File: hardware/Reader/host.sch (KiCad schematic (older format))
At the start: 7 parts

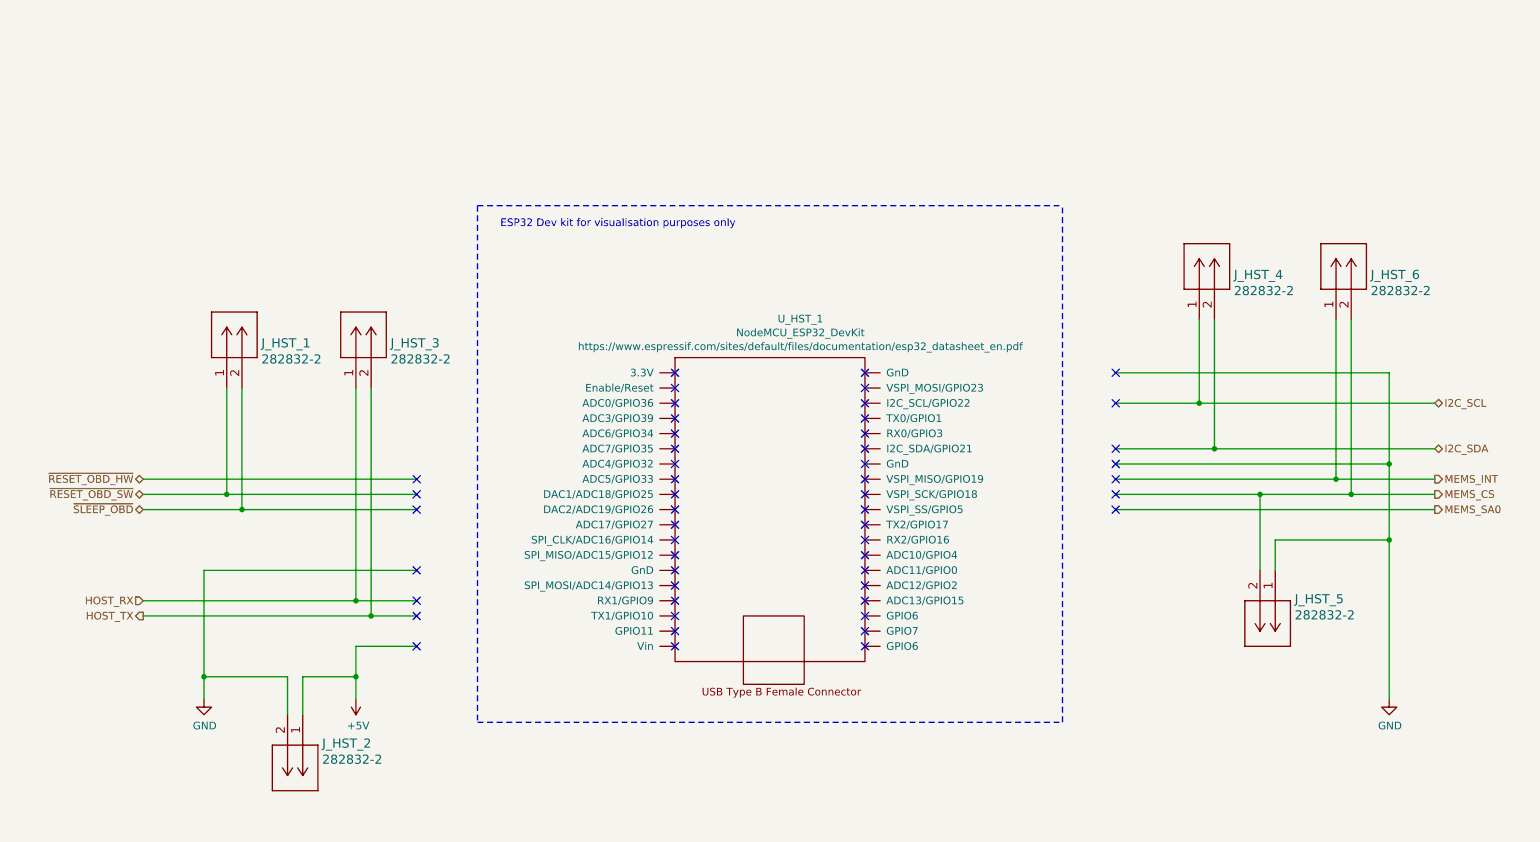
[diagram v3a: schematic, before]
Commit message: Fixed minor bugs in schematic. Completed PCB layout v0.0.1 and exported Gerber files
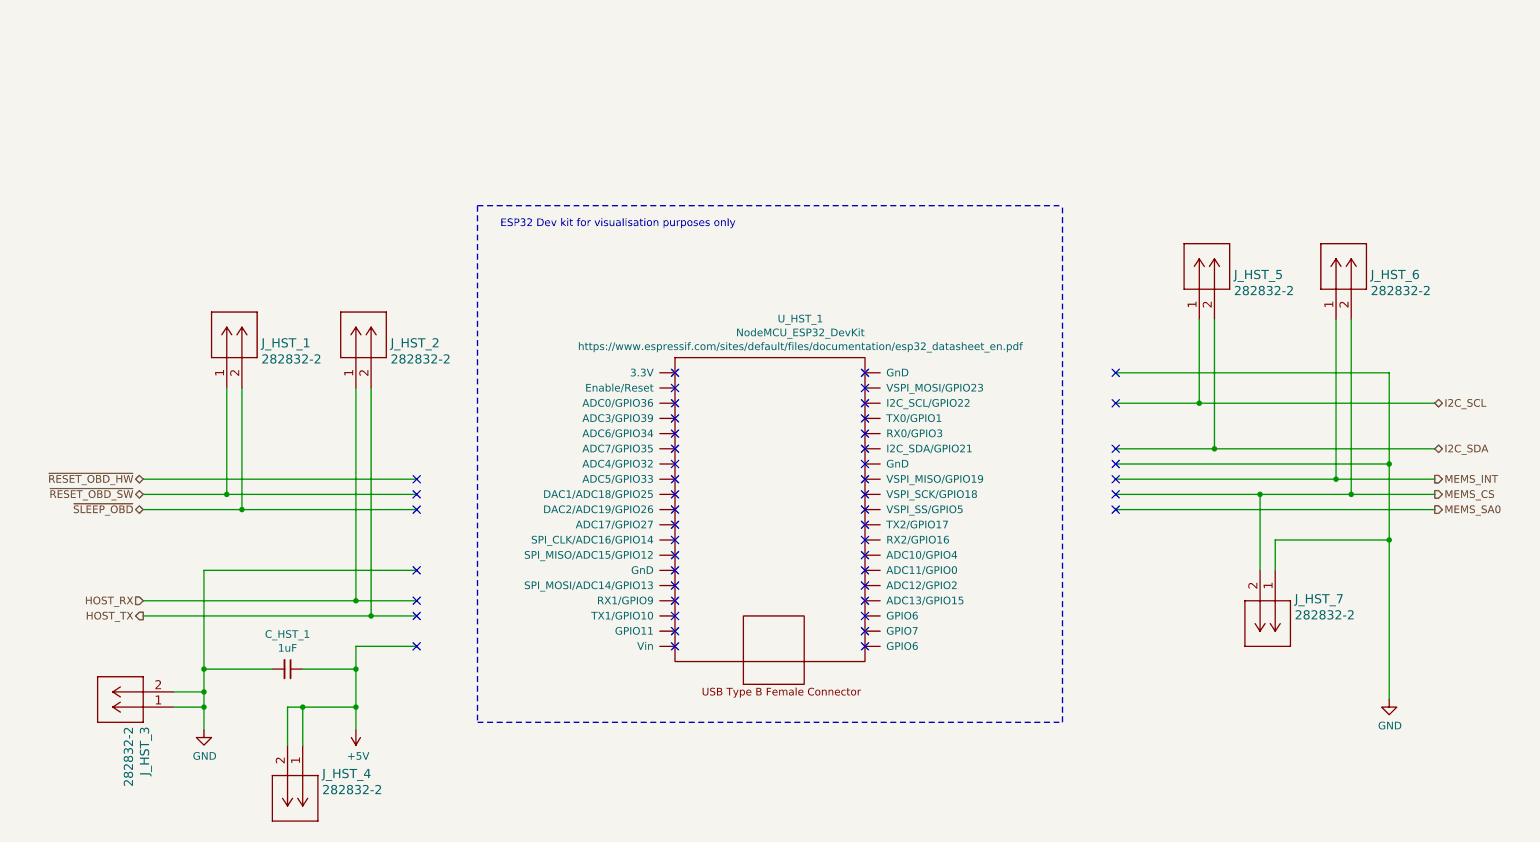
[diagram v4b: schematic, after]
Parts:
- added C_HST_1: 1uF, footprints:0603, symbol Device:C_Small
- added J_HST_3: 282832-2, footprints:282832-2, symbol 2828322:282832-2
- renumbered J_HST_3 to J_HST_2, J_HST_2 to J_HST_4, J_HST_4 to J_HST_5, J_HST_5 to J_HST_7
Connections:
- net +5V: now also J_HST_4.2, C_HST_1.1
- net GND: now also C_HST_1.2, J_HST_3.1, J_HST_3.2; no longer J_HST_4.2
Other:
- moved on the sheet: J_HST_4
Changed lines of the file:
@@
 Sheet 13 19
 Title "CANnect Reader | Host"
-Date "2020-10-25"
+Date "2020-10-27"
 Rev "0.0.03"
 Comp "CANtech"
@@
 L power:GND #PWR084
 U 1 1 5F91E8F3
-P 1800 5400
-F 0 "#PWR084" H 1800 5150 50  0001 C CNN
-F 1 "GND" H 1805 5227 50  0000 C CNN
-F 2 "" H 1800 5400 50  0001 C CNN
-F 3 "" H 1800 5400 50  0001 C CNN
-	1    1800 5400
+P 1800 5600
+F 0 "#PWR084" H 1800 5350 50  0001 C CNN
+F 1 "GND" H 1805 5427 50  0000 C CNN
+F 2 "" H 1800 5600 50  0001 C CNN
+F 3 "" H 1800 5600 50  0001 C CNN
+	1    1800 5600
 	1    0    0    -1
 $EndComp
-Wire Wire Line
-	1800 5400 1800 5250
 $Comp
 L power:+5V #PWR085
 U 1 1 5F91DA5E
-P 2800 5400
-F 0 "#PWR085" H 2800 5250 50  0001 C CNN
-F 1 "+5V" H 2815 5573 50  0000 C CNN
-F 2 "" H 2800 5400 50  0001 C CNN
-F 3 "" H 2800 5400 50  0001 C CNN
-	1    2800 5400
+P 2800 5600
+F 0 "#PWR085" H 2800 5450 50  0001 C CNN
+F 1 "+5V" H 2815 5773 50  0000 C CNN
+F 2 "" H 2800 5600 50  0001 C CNN
+F 3 "" H 2800 5600 50  0001 C CNN
+	1    2800 5600
 	1    0    0    1
 $EndComp
 Wire Wire Line
-	2800 5400 2800 5250
+	2800 5600 2800 5450
 $Comp
 L CANtech:NodeMCU_ESP32_DevKit U_HST_?
@@
 $EndComp
 Wire Wire Line
-	2800 5050 3200 5050
-Wire Wire Line
 	1800 4550 3200 4550
 NoConn ~ 3200 3950
@@
 $EndComp
 $Comp
-L 2828322:282832-2 J_HST_3
+L 2828322:282832-2 J_HST_2
 U 1 1 5F9D9258
 P 2800 3350
-F 0 "J_HST_3" V 3095 3122 60  0000 R CNN
+F 0 "J_HST_2" V 3095 3122 60  0000 R CNN
 F 1 "282832-2" V 2989 3122 60  0000 R CNN
 F 2 "footprints:282832-2" H 3200 3290 60  0001 C CNN
@@
 $EndComp
 $Comp
-L 2828322:282832-2 J_HST_2
+L 2828322:282832-2 J_HST_4
 U 1 1 5F9D9519
-P 2450 5500
-F 0 "J_HST_2" V 2639 5628 60  0000 L CNN
-F 1 "282832-2" V 2745 5628 60  0000 L CNN
-F 2 "footprints:282832-2" H 2850 5440 60  0001 C CNN
-F 3 "https://www.te.com/commerce/DocumentDelivery/DDEController?Action=srchrtrv&DocNm=282832&DocType=Customer+Drawing&DocLang=English" H 2450 5500 60  0001 C CNN
-F 4 "282832-2" H 2450 5500 50  0001 C CNN "Part Name"
-F 5 "DigiKey Canada" H 2450 5500 50  0001 C CNN "Vendor"
-F 6 "TE Connectivity AMP Connectors" H 2450 5500 50  0001 C CNN "Manufacturer"
-F 7 "A113314-ND" H 2450 5500 50  0001 C CNN "digikeypn"
-	1    2450 5500
+P 2450 5700
+F 0 "J_HST_4" V 2639 5828 60  0000 L CNN
+F 1 "282832-2" V 2745 5828 60  0000 L CNN
+F 2 "footprints:282832-2" H 2850 5640 60  0001 C CNN
+F 3 "https://www.te.com/commerce/DocumentDelivery/DDEController?Action=srchrtrv&DocNm=282832&DocType=Customer+Drawing&DocLang=English" H 2450 5700 60  0001 C CNN
+F 4 "282832-2" H 2450 5700 50  0001 C CNN "Part Name"
+F 5 "DigiKey Canada" H 2450 5700 50  0001 C CNN "Vendor"
+F 6 "TE Connectivity AMP Connectors" H 2450 5700 50  0001 C CNN "Manufacturer"
+F 7 "A113314-ND" H 2450 5700 50  0001 C CNN "digikeypn"
+	1    2450 5700
 	0    1    1    0
 $EndComp
 $Comp
-L 2828322:282832-2 J_HST_4
+L 2828322:282832-2 J_HST_5
 U 1 1 5F9DA91B
 P 8350 2900
-F 0 "J_HST_4" V 8645 2672 60  0000 R CNN
+F 0 "J_HST_5" V 8645 2672 60  0000 R CNN
 F 1 "282832-2" V 8539 2672 60  0000 R CNN
 F 2 "footprints:282832-2" H 8750 2840 60  0001 C CNN
@@
 NoConn ~ 7800 3950
 Wire Wire Line
-	2450 5500 2450 5250
-Wire Wire Line
-	2450 5250 2800 5250
-Connection ~ 2800 5250
-Wire Wire Line
-	2800 5250 2800 5050
-Wire Wire Line
-	2350 5500 2350 5250
-Wire Wire Line
-	2350 5250 1800 5250
-Connection ~ 1800 5250
-Wire Wire Line
-	1800 5250 1800 4550
+	2450 5700 2450 5450
 Wire Notes Line
 	3600 2150 3600 5550
@@
 	7800 4150 9900 4150
 $Comp
-L 2828322:282832-2 J_HST_5
+L 2828322:282832-2 J_HST_7
 U 1 1 5F9F4BEC
 P 8850 4550
-F 0 "J_HST_5" V 9039 4678 60  0000 L CNN
+F 0 "J_HST_7" V 9039 4678 60  0000 L CNN
 F 1 "282832-2" V 9145 4678 60  0000 L CNN
 F 2 "footprints:282832-2" H 9250 4490 60  0001 C CNN
@@
 NoConn ~ 6150 3350
 NoConn ~ 6150 3250
+$Comp
+L Device:C_Small C_HST_1
+U 1 1 5FB5FEEA
+P 2350 5200
+F 0 "C_HST_1" V 2121 5200 50  0000 C CNN
+F 1 "1uF" V 2212 5200 50  0000 C CNN
+F 2 "footprints:0603" H 2350 5200 50  0001 C CNN
+F 3 "https://content.kemet.com/datasheets/KEM_C1002_X7R_SMD.pdf" H 2350 5200 50  0001 C CNN
+F 4 "Kermet" H 2350 5200 50  0001 C CNN "Manufacturer"
+F 5 "C0603C105K4RACTU" H 2350 5200 50  0001 C CNN "Part Name"
+F 6 "DigiKey Canada" H 2350 5200 50  0001 C CNN "Vendor"
+F 7 "399-7847-1-ND" H 2350 5200 50  0001 C CNN "digikeypn"
+	1    2350 5200
+	0    1    1    0
+$EndComp
+Wire Wire Line
+	2800 5050 3200 5050
+Wire Wire Line
+	2450 5450 2800 5450
+Wire Wire Line
+	1800 4550 1800 5200
+Wire Wire Line
+	2800 5050 2800 5200
+Connection ~ 2800 5450
+$Comp
+L 2828322:282832-2 J_HST_3
+U 1 1 5FB693E7
+P 1600 5450
+F 0 "J_HST_3" V 1789 5578 60  0000 L CNN
+F 1 "282832-2" V 1895 5578 60  0000 L CNN
+F 2 "footprints:282832-2" H 2000 5390 60  0001 C CNN
+F 3 "https://www.te.com/commerce/DocumentDelivery/DDEController?Action=srchrtrv&DocNm=282832&DocType=Customer+Drawing&DocLang=English" H 1600 5450 60  0001 C CNN
+F 4 "282832-2" H 1600 5450 50  0001 C CNN "Part Name"
+F 5 "DigiKey Canada" H 1600 5450 50  0001 C CNN "Vendor"
+F 6 "TE Connectivity AMP Connectors" H 1600 5450 50  0001 C CNN "Manufacturer"
+F 7 "A113314-ND" H 1600 5450 50  0001 C CNN "digikeypn"
+	1    1600 5450
+	-1   0    0    1
+$EndComp
+Wire Wire Line
+	1600 5450 1800 5450
+Connection ~ 1800 5450
+Wire Wire Line
+	1800 5450 1800 5600
+Wire Wire Line
+	2450 5200 2800 5200
+Connection ~ 2800 5200
+Wire Wire Line
+	2800 5200 2800 5450
+Wire Wire Line
+	2250 5200 1800 5200
+Connection ~ 1800 5200
+Wire Wire Line
+	1800 5200 1800 5350
+Wire Wire Line
+	1600 5350 1800 5350
+Connection ~ 1800 5350
+Wire Wire Line
+	1800 5350 1800 5450
+Wire Wire Line
+	2350 5700 2350 5450
+Wire Wire Line
+	2350 5450 2450 5450
+Connection ~ 2450 5450
 $EndSCHEMATC

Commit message: Fixed bugs in schematic. Updated BOM list. Swapped to using ESP32 holder. Updated PCB layout to v0.0.2. Updated schematic to v0.0.4
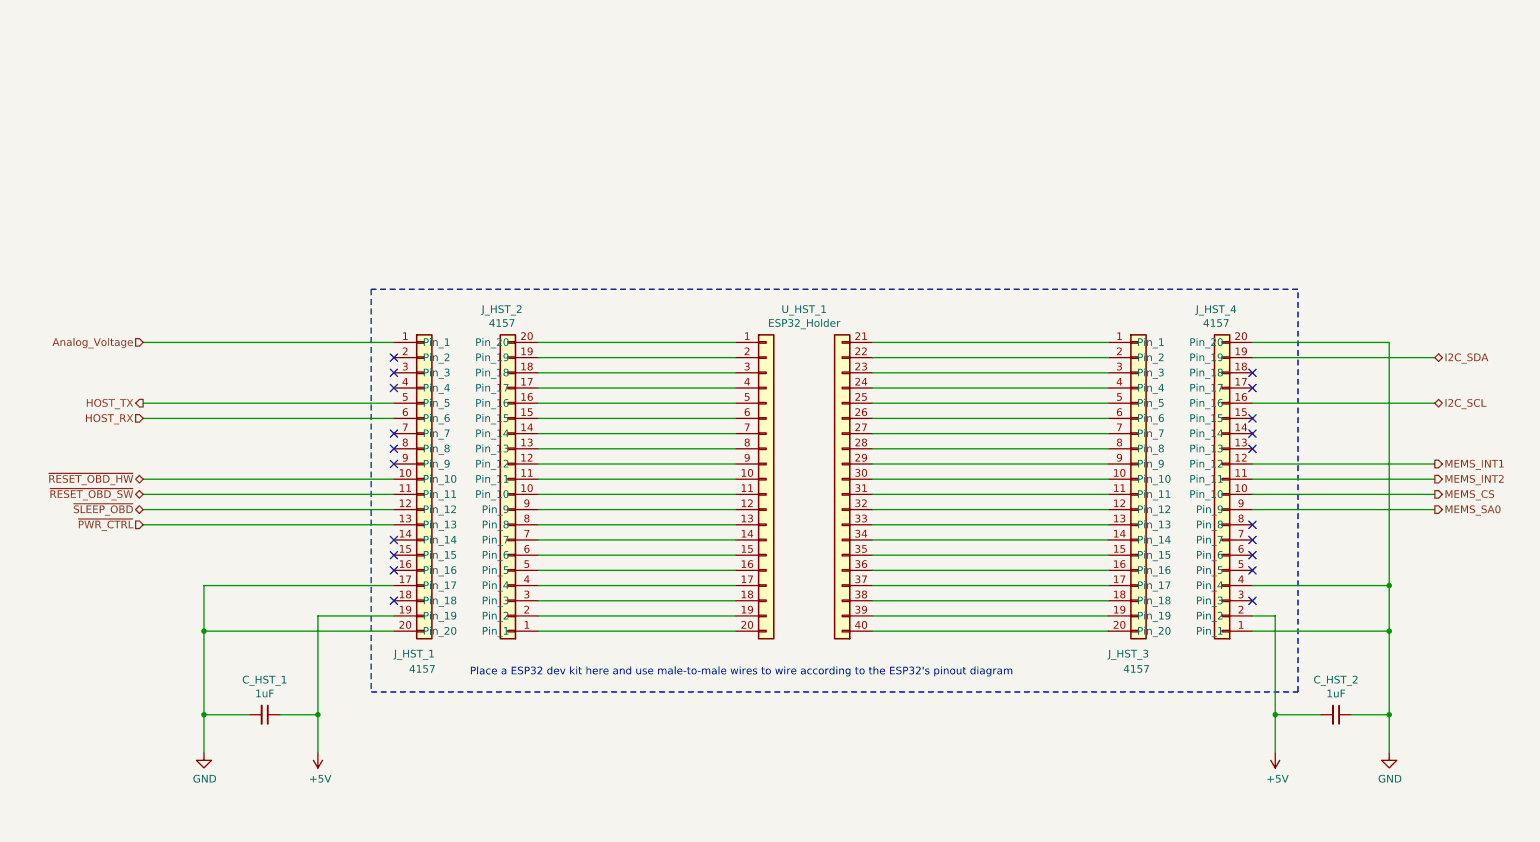
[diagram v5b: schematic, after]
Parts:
- removed J_HST_1, J_HST_2, J_HST_3, J_HST_4, J_HST_5, J_HST_6, J_HST_7: 282832-2, footprints:282832-2, symbol 2828322:282832-2
- removed U_HST_1: NodeMCU_ESP32_DevKit, symbol CANtech:NodeMCU_ESP32_DevKit
- added C_HST_2: 1uF, footprints:0603, symbol Device:C_Small
- added J_HST_1, J_HST_2, J_HST_3, J_HST_4: 4157, Connector_PinSocket_2.54mm:PinSocket_1x20_P2.54mm_Vertical, symbol CANtech:4157
- added U_HST_1: ESP32_Holder, footprints:ESP32_Holder, symbol CANtech:ESP32_Holder
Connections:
- net +5V: now also C_HST_2.2, J_HST_1.19 (Pin_19), J_HST_4.2 (Pin_2)
- net GND: now also C_HST_2.1, J_HST_1.17 (Pin_17), J_HST_1.20 (Pin_20), J_HST_4.1 (Pin_1), J_HST_4.20 (Pin_20), J_HST_4.4 (Pin_4)
- net HOST_RX: now also J_HST_1.6 (Pin_6)
- net HOST_TX: now also J_HST_1.5 (Pin_5)
- net I2C_SCL: now also J_HST_4.16 (Pin_16)
- net I2C_SDA: now also J_HST_4.19 (Pin_19)
- net MEMS_CS: now also J_HST_4.10 (Pin_10)
- net MEMS_SA0: now also J_HST_4.9 (Pin_9)
- net ~RESET_OBD_HW~: now also J_HST_1.10 (Pin_10)
- net ~RESET_OBD_SW~: now also J_HST_1.11 (Pin_11)
- net ~SLEEP_OBD~: now also J_HST_1.12 (Pin_12)
- new net: J_HST_2.20 (Pin_20), U_HST_1.1 (Pin_1)
- new net: J_HST_2.11 (Pin_11), U_HST_1.10 (Pin_10)
- new net: J_HST_2.10 (Pin_10), U_HST_1.11 (Pin_11)
- new net: J_HST_2.9 (Pin_9), U_HST_1.12 (Pin_12)
- new net: J_HST_2.8 (Pin_8), U_HST_1.13 (Pin_13)
- new net: J_HST_2.7 (Pin_7), U_HST_1.14 (Pin_14)
- new net: J_HST_2.6 (Pin_6), U_HST_1.15 (Pin_15)
- new net: J_HST_2.5 (Pin_5), U_HST_1.16 (Pin_16)
- new net: J_HST_2.4 (Pin_4), U_HST_1.17 (Pin_17)
- new net: J_HST_2.3 (Pin_3), U_HST_1.18 (Pin_18)
- new net: J_HST_2.2 (Pin_2), U_HST_1.19 (Pin_19)
- new net: J_HST_2.19 (Pin_19), U_HST_1.2 (Pin_2)
- new net: J_HST_2.1 (Pin_1), U_HST_1.20 (Pin_20)
- new net: J_HST_3.1 (Pin_1), U_HST_1.21 (Pin_21)
- new net: J_HST_3.2 (Pin_2), U_HST_1.22 (Pin_22)
- new net: J_HST_3.3 (Pin_3), U_HST_1.23 (Pin_23)
- new net: J_HST_3.4 (Pin_4), U_HST_1.24 (Pin_24)
- new net: J_HST_3.5 (Pin_5), U_HST_1.25 (Pin_25)
- new net: J_HST_3.6 (Pin_6), U_HST_1.26 (Pin_26)
- new net: J_HST_3.7 (Pin_7), U_HST_1.27 (Pin_27)
- new net: J_HST_3.8 (Pin_8), U_HST_1.28 (Pin_28)
- new net: J_HST_3.9 (Pin_9), U_HST_1.29 (Pin_29)
- new net: J_HST_2.18 (Pin_18), U_HST_1.3 (Pin_3)
- new net: J_HST_3.10 (Pin_10), U_HST_1.30 (Pin_30)
- new net: J_HST_3.11 (Pin_11), U_HST_1.31 (Pin_31)
- new net: J_HST_3.12 (Pin_12), U_HST_1.32 (Pin_32)
- new net: J_HST_3.13 (Pin_13), U_HST_1.33 (Pin_33)
- new net: J_HST_3.14 (Pin_14), U_HST_1.34 (Pin_34)
- new net: J_HST_3.15 (Pin_15), U_HST_1.35 (Pin_35)
- new net: J_HST_3.16 (Pin_16), U_HST_1.36 (Pin_36)
- new net: J_HST_3.17 (Pin_17), U_HST_1.37 (Pin_37)
- new net: J_HST_3.18 (Pin_18), U_HST_1.38 (Pin_38)
- new net: J_HST_3.19 (Pin_19), U_HST_1.39 (Pin_39)
- new net: J_HST_2.17 (Pin_17), U_HST_1.4 (Pin_4)
- new net: J_HST_3.20 (Pin_20), U_HST_1.40 (Pin_40)
- new net: J_HST_2.16 (Pin_16), U_HST_1.5 (Pin_5)
- new net: J_HST_2.15 (Pin_15), U_HST_1.6 (Pin_6)
- new net: J_HST_2.14 (Pin_14), U_HST_1.7 (Pin_7)
- new net: J_HST_2.13 (Pin_13), U_HST_1.8 (Pin_8)
- new net: J_HST_2.12 (Pin_12), U_HST_1.9 (Pin_9)
- new net Analog_Voltage: J_HST_1.1 (Pin_1)
- new net MEMS_INT1: J_HST_4.12 (Pin_12)
- new net MEMS_INT2: J_HST_4.11 (Pin_11)
- new net ~PWR_CTRL~: J_HST_1.13 (Pin_13)
- no-connect marks 52 -> 20
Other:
- note added: "Place a ESP32 dev kit here and use male-to-male wires to wire according to the ESP32's pinout diagram"
- note removed: "ESP32 Dev kit for visualisation purposes only"
- moved on the sheet: C_HST_1

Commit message: Fixed a component name for header pin
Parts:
- J_HST_1, J_HST_2, J_HST_3, J_HST_4: Part Name (none) -> 4157
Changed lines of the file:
@@
 F 5 "Adafruit Industries LLC" H 3200 3450 50  0001 C CNN "Manufacturer"
 F 6 "1528-2929-ND" H 3200 3450 50  0001 C CNN "digikeypn"
+F 7 "4157" H 3200 3450 50  0001 C CNN "Part Name"
 	1    3200 3450
 	1    0    0    -1
@@
 F 5 "Adafruit Industries LLC" H 3850 4550 50  0001 C CNN "Manufacturer"
 F 6 "1528-2929-ND" H 3850 4550 50  0001 C CNN "digikeypn"
+F 7 "4157" H 3850 4550 50  0001 C CNN "Part Name"
 	1    3850 4550
 	-1   0    0    1
@@
 F 5 "Adafruit Industries LLC" H 8550 4550 50  0001 C CNN "Manufacturer"
 F 6 "1528-2929-ND" H 8550 4550 50  0001 C CNN "digikeypn"
+F 7 "4157" H 8550 4550 50  0001 C CNN "Part Name"
 	1    8550 4550
 	-1   0    0    1
@@
 F 5 "Adafruit Industries LLC" H 7900 3450 50  0001 C CNN "Manufacturer"
 F 6 "1528-2929-ND" H 7900 3450 50  0001 C CNN "digikeypn"
+F 7 "4157" H 7900 3450 50  0001 C CNN "Part Name"
 	1    7900 3450
 	1    0    0    -1

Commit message: Revising reader
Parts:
- removed C_HST_2: 1uF, footprints:0603, symbol Device:C_Small
- removed J_HST_3, J_HST_4: 4157, Connector_PinSocket_2.54mm:PinSocket_1x20_P2.54mm_Vertical, symbol CANtech:4157
- removed U_HST_1: ESP32_Holder, footprints:ESP32_Holder, symbol CANtech:ESP32_Holder
- added CP_HST_1: 100uF, symbol Device:CP
- added R_HST_?: 100k, footprints:RESC1608X55N, symbol Device:R_Small
- added U_HST_1: ESP32-WROOM-32D, RF_Module:ESP32-WROOM-32, symbol RF_Module:ESP32-WROOM-32D
- J_HST_1, J_HST_2: Part Name 4157 -> (none)
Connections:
- net Analog_Voltage: no longer J_HST_1.1 (Pin_1)
- net GND: now also J_HST_1.1 (Pin_1), CP_HST_1.2, U_HST_1.1 (GND), U_HST_1.15 (GND), U_HST_1.38 (GND), U_HST_1.39 (GND); no longer J_HST_1.17 (Pin_17), J_HST_1.20 (Pin_20)
- net HOST_RX: now also U_HST_1.27 (IO16); no longer J_HST_1.6 (Pin_6)
- net HOST_TX: now also U_HST_1.28 (IO17); no longer J_HST_1.5 (Pin_5)
- net ~PWR_CTRL~: no longer J_HST_1.13 (Pin_13)
- net ~RESET_OBD_HW~: no longer J_HST_1.10 (Pin_10)
- net ~RESET_OBD_SW~: no longer J_HST_1.11 (Pin_11)
- net ~SLEEP_OBD~: no longer J_HST_1.12 (Pin_12)
- net at J_HST_1.18 (Pin_18): now also U_HST_1.5 (SENSOR_VN)
- net +5V: no longer names the net of J_HST_1.19 (Pin_19)
- net +5V: now also U_HST_1.4 (SENSOR_VP); no longer C_HST_1.1
- new net: R_HST_?.1, U_HST_1.3 (EN)
- new net +3V3: CP_HST_1.1, C_HST_1.1, J_HST_1.20 (Pin_20), R_HST_?.2, U_HST_1.2 (VDD)
- no-connect marks 20 -> 0
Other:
- note added: "Head Jumpers"
- note removed: "Place a ESP32 dev kit here and use male-to-male wires to wire according to the ESP32's pinout diagram"
- moved on the sheet: C_HST_1
